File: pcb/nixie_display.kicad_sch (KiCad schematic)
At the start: 12 parts, among them U1 IC_SR_MC_HV5622PG-G, U2 IC_SR_MC_HV5622PG-G

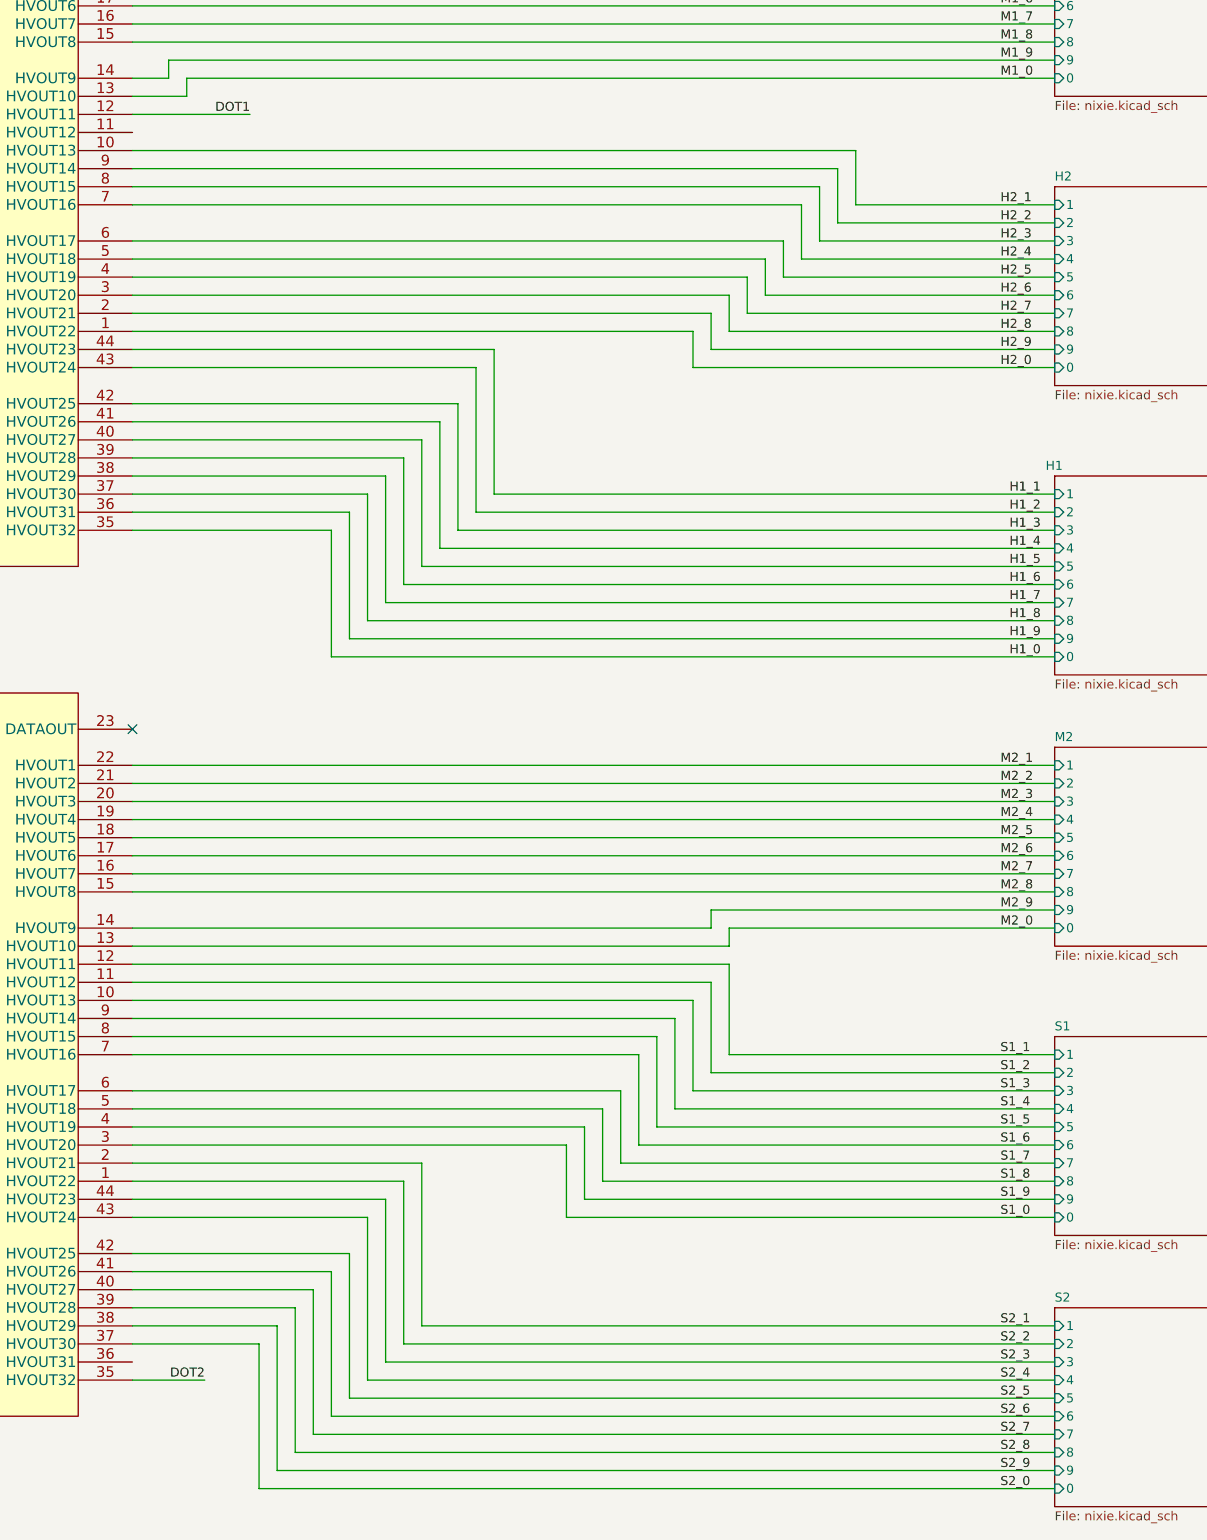
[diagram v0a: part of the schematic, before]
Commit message: Reshuffled Nixie page some more to make routing cleaner
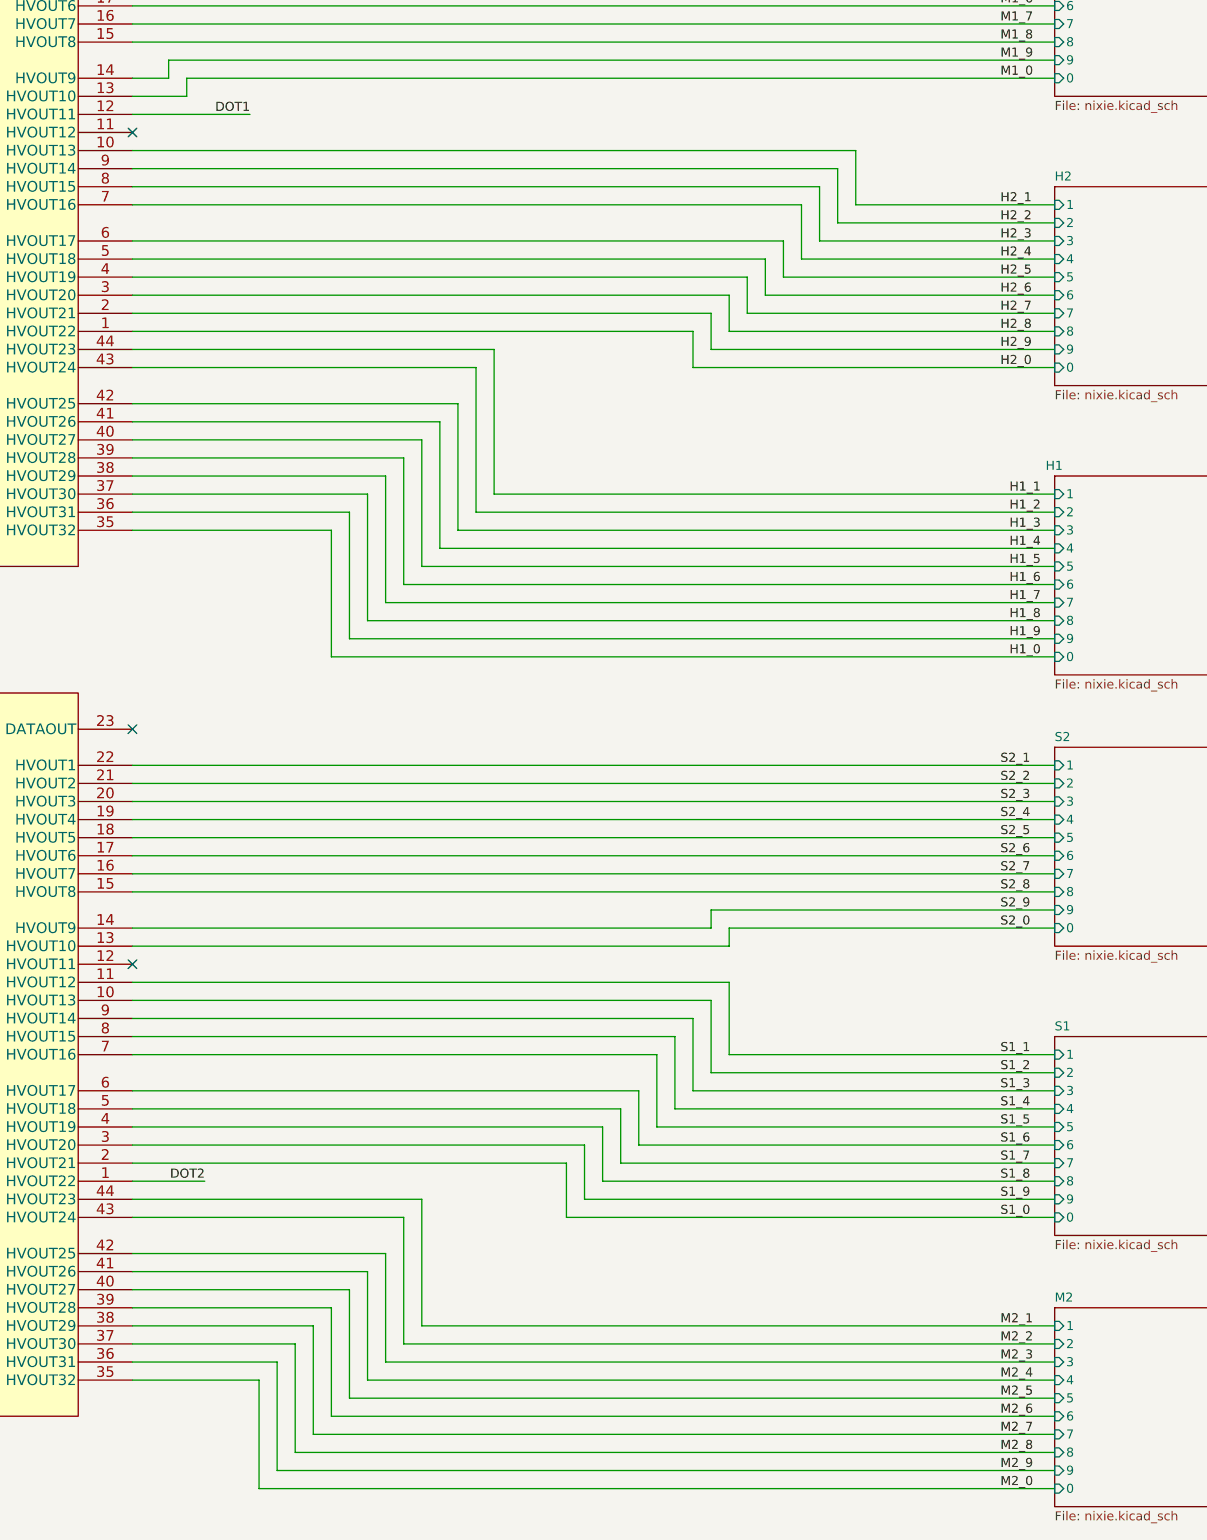
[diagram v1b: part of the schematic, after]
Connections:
- net DOT2: now also U2.1 (HVOUT22); no longer U2.35 (HVOUT32)
- net M2_0: now also U2.35 (HVOUT32); no longer U2.13 (HVOUT10)
- net M2_1: now also U2.44 (HVOUT23); no longer U2.22 (HVOUT1)
- net M2_2: now also U2.43 (HVOUT24); no longer U2.21 (HVOUT2)
- net M2_3: now also U2.42 (HVOUT25); no longer U2.20 (HVOUT3)
- net M2_4: now also U2.41 (HVOUT26); no longer U2.19 (HVOUT4)
- net M2_5: now also U2.40 (HVOUT27); no longer U2.18 (HVOUT5)
- net M2_6: now also U2.39 (HVOUT28); no longer U2.17 (HVOUT6)
- net M2_7: now also U2.38 (HVOUT29); no longer U2.16 (HVOUT7)
- net M2_8: now also U2.37 (HVOUT30); no longer U2.15 (HVOUT8)
- net M2_9: now also U2.36 (HVOUT31); no longer U2.14 (HVOUT9)
- net S1_0: now also U2.2 (HVOUT21); no longer U2.3 (HVOUT20)
- net S1_1: now also U2.11 (HVOUT12); no longer U2.12 (HVOUT11)
- net S1_2: now also U2.10 (HVOUT13); no longer U2.11 (HVOUT12)
- net S1_3: now also U2.9 (HVOUT14); no longer U2.10 (HVOUT13)
- net S1_4: now also U2.8 (HVOUT15); no longer U2.9 (HVOUT14)
- net S1_5: now also U2.7 (HVOUT16); no longer U2.8 (HVOUT15)
- net S1_6: now also U2.6 (HVOUT17); no longer U2.7 (HVOUT16)
- net S1_7: now also U2.5 (HVOUT18); no longer U2.6 (HVOUT17)
- net S1_8: now also U2.4 (HVOUT19); no longer U2.5 (HVOUT18)
- net S1_9: now also U2.3 (HVOUT20); no longer U2.4 (HVOUT19)
- net S2_0: now also U2.13 (HVOUT10); no longer U2.37 (HVOUT30)
- net S2_1: now also U2.22 (HVOUT1); no longer U2.2 (HVOUT21)
- net S2_2: now also U2.21 (HVOUT2); no longer U2.1 (HVOUT22)
- net S2_3: now also U2.20 (HVOUT3); no longer U2.44 (HVOUT23)
- net S2_4: now also U2.19 (HVOUT4); no longer U2.43 (HVOUT24)
- net S2_5: now also U2.18 (HVOUT5); no longer U2.42 (HVOUT25)
- net S2_6: now also U2.17 (HVOUT6); no longer U2.41 (HVOUT26)
- net S2_7: now also U2.16 (HVOUT7); no longer U2.40 (HVOUT27)
- net S2_8: now also U2.15 (HVOUT8); no longer U2.39 (HVOUT28)
- net S2_9: now also U2.14 (HVOUT9); no longer U2.38 (HVOUT29)
- no-connect marks 1 -> 3

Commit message: Some minor tweaks and generated gerbers
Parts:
- N1, N2: now not fitted
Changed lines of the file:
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@@
 		(in_bom yes)
 		(on_board yes)
-		(dnp no)
+		(dnp yes)
 		(property "Reference" "N1"
 			(at 340.36 119.38 0)
@@
 		(in_bom yes)
 		(on_board yes)
-		(dnp no)
+		(dnp yes)
 		(property "Reference" "N2"
 			(at 340.36 137.16 0)

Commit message: Realized I got my tube naming backwards. Updated schematic with correct naming annotations
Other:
- note added: "Also realizing I made a booboo with the layout! I put hours on the "left" and seconds on the "right" in layout"
- note added: "H1 TUBE 0"
- note added: "H2 TUBE 1"
- note added: "M1 TUBE 2"
- note added: "M2 TUBE 3"
- note added: "S1 TUBE 4"
- note added: "S2 TUBE 5"
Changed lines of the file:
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@@
+		)
+	)
+	(text_box "Also realizing I made a booboo with the layout! I put hours on the \"left\" and seconds on the \"right\" in layout... but the layout is \"looking outward\" meaning the order is actually inverterted.\n\nH1 == S2\nH2 == S1\nM1 == M2\nM2 == M1\nS1 == H2\nS2 == H1"
+		(exclude_from_sim no)
+		(at 309.88 20.32 0)
+		(size 38.1 33.02)
+		(stroke
+			(width 0)
+			(type default)
+		)
+		(fill
+			(type none)
+		)
+		(effects
+			(font
+				(size 1.27 1.27)
+			)
+			(justify left top)
+		)
+	)
+	(text "H2\nTUBE 1"
+		(exclude_from_sim no)
+		(at 265.684 215.392 0)
+		(effects
+			(font
+				(size 3.81 3.81)
+				(thickness 5.08)
+				(bold yes)
+				(color 255 65 243 1)
+			)
 		)
 	)
@@
 			)
 			(justify left bottom)
+		)
+	)
+	(text "Also realizing I made a booboo with the layout! I put hours on the \"left\" and seconds on the \"right\" in layout"
+		(exclude_from_sim no)
+		(at 0 0 0)
+		(effects
+			(font
+				(size 1.27 1.27)
+			)
+		)
+	)
+	(text "H1\nTUBE 0"
+		(exclude_from_sim no)
+		(at 266.446 173.99 0)
+		(effects
+			(font
+				(size 3.81 3.81)
+				(thickness 5.08)
+				(bold yes)
+				(color 255 65 243 1)
+			)
+		)
+	)
+	(text "M2\nTUBE 3"
+		(exclude_from_sim no)
+		(at 265.43 54.356 0)
+		(effects
+			(font
+				(size 3.81 3.81)
+				(thickness 5.08)
+				(bold yes)
+				(color 255 65 243 1)
+			)
 		)
 	)
@@
 		)
 	)
+	(text "S2\nTUBE 5"
+		(exclude_from_sim no)
+		(at 265.684 136.906 0)
+		(effects
+			(font
+				(size 3.81 3.81)
+				(thickness 5.08)
+				(bold yes)
+				(color 255 65 243 1)
+			)
+		)
+	)
+	(text "S1\nTUBE 4"
+		(exclude_from_sim no)
+		(at 265.684 95.758 0)
+		(effects
+			(font
+				(size 3.81 3.81)
+				(thickness 5.08)
+				(bold yes)
+				(color 255 65 243 1)
+			)
+		)
+	)
+	(text "M1\nTUBE 2"
+		(exclude_from_sim no)
+		(at 266.192 253.746 0)
+		(effects
+			(font
+				(size 3.81 3.81)
+				(thickness 5.08)
+				(bold yes)
+				(color 255 65 243 1)
+			)
+		)
+	)
